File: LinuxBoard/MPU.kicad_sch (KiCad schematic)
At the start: 28 parts, among them J2 Conn_02x10_Counter_Clockwise, J3 Micro_SD_Card, J4 USB_A, SW1 SW_DIP_x03, SW2 SW_Push, SW3 SW_Push, U1 STM32MP151AAB3, Y1 24MHz, Y2 32.768KHz

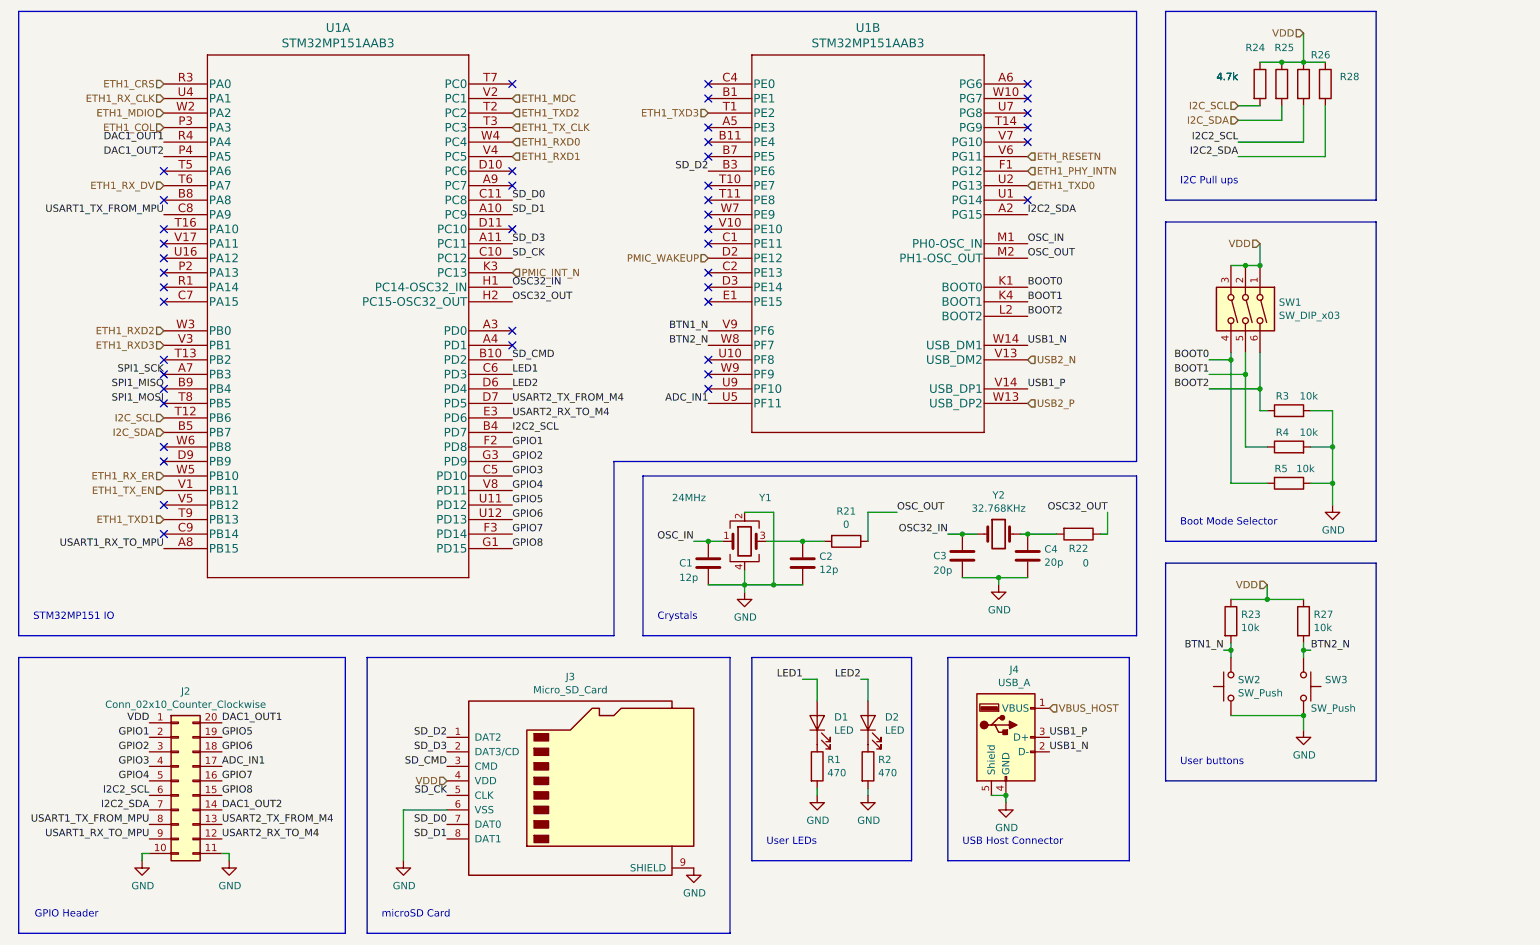
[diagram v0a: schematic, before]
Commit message: Fix ERC errors and reorganize directory
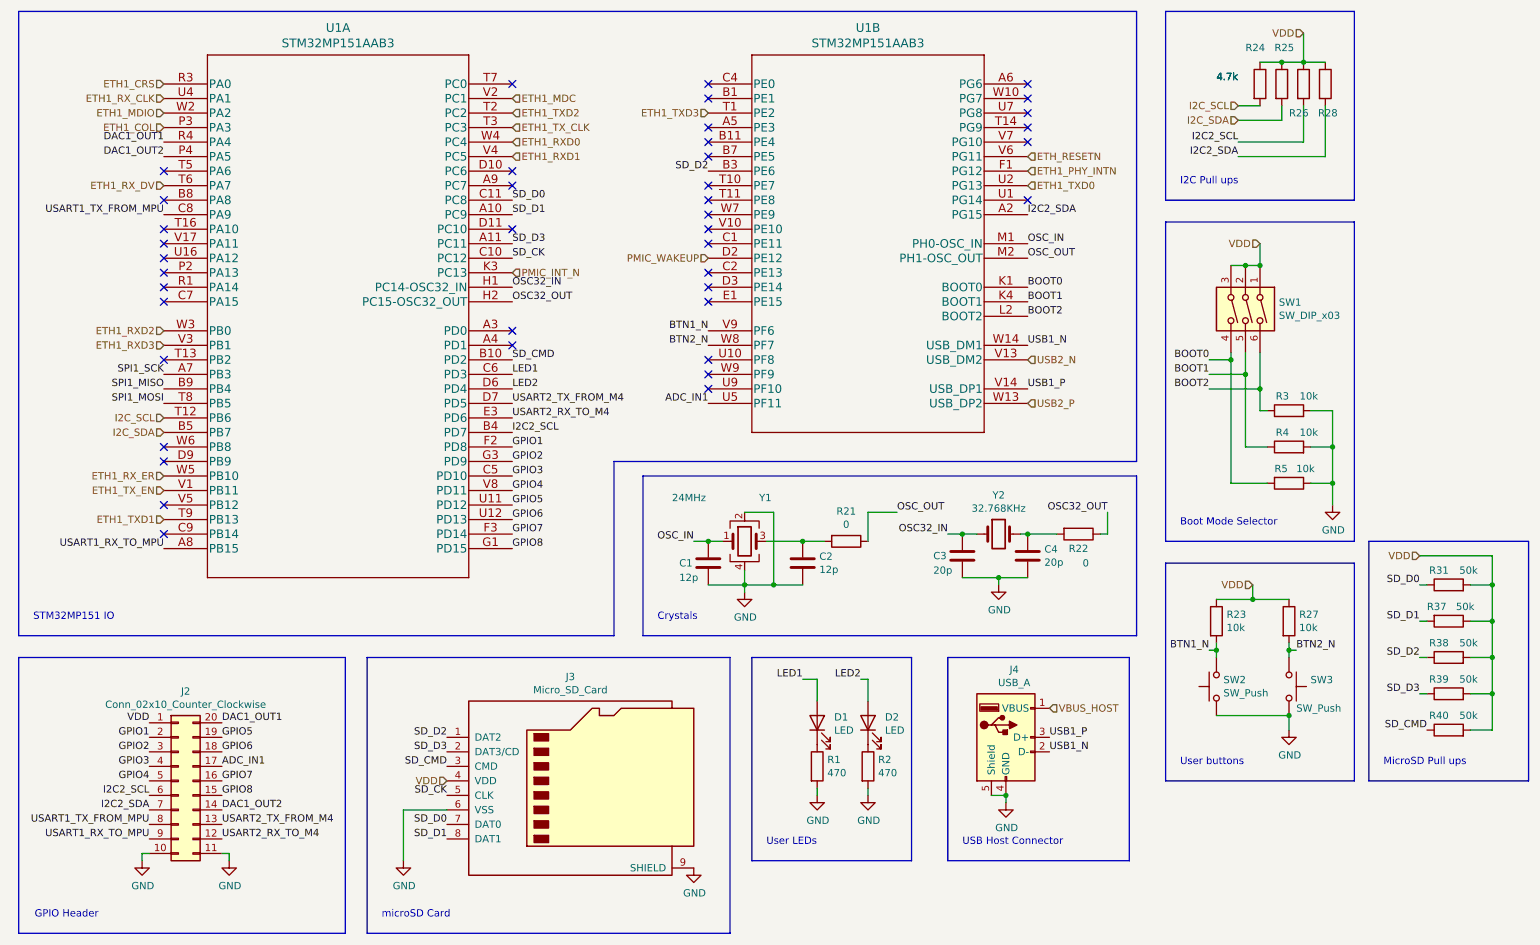
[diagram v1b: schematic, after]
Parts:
- added R31, R37, R38, R39, R40: 50k, Resistor_SMD:R_0603_1608Metric_Pad0.98x0.95mm_HandSolder, symbol Device:R
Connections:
- net SD_CMD: now also R40.1
- net SD_D0: now also R31.1
- net SD_D1: now also R37.2
- net SD_D2: now also R38.1
- net SD_D3: now also R39.1
- net VDD: now also R31.2, R37.1, R38.2, R39.2, R40.2
- no-connect marks 44 -> 41
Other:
- note added: "MicroSD Pull ups"
- moved on the sheet: R23, R27, SW2, SW3

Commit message: Fix resistor footprints, restart layout
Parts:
- R1, R2, R21, R22, R23, R24, R25, R26, R27, R28, R3, R4, R5: footprint Resistor_SMD:R_0603_1608Metric_Pad1.05x0.95mm_HandSolder -> Resistor_SMD:R_0603_1608Metric_Pad0.98x0.95mm_HandSolder
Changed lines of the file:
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@@
       (effects (font (size 1.27 1.27)) (justify left))
     )
-    (property "Footprint" "Resistor_SMD:R_0603_1608Metric_Pad1.05x0.95mm_HandSolder" (id 2) (at 241.3 94.742 90)
+    (property "Footprint" "Resistor_SMD:R_0603_1608Metric_Pad0.98x0.95mm_HandSolder" (id 2) (at 241.3 94.742 90)
       (effects (font (size 1.27 1.27)) hide)
     )
@@
       (effects (font (size 1.27 1.27)) (justify left))
     )
-    (property "Footprint" "Resistor_SMD:R_0603_1608Metric_Pad1.05x0.95mm_HandSolder" (id 2) (at 241.3 91.948 90)
+    (property "Footprint" "Resistor_SMD:R_0603_1608Metric_Pad0.98x0.95mm_HandSolder" (id 2) (at 241.3 91.948 90)
       (effects (font (size 1.27 1.27)) hide)
     )
@@
       (effects (font (size 1.27 1.27)) (justify left))
     )
-    (property "Footprint" "Resistor_SMD:R_0603_1608Metric_Pad1.05x0.95mm_HandSolder" (id 2) (at 241.3 85.598 90)
+    (property "Footprint" "Resistor_SMD:R_0603_1608Metric_Pad0.98x0.95mm_HandSolder" (id 2) (at 241.3 85.598 90)
       (effects (font (size 1.27 1.27)) hide)
     )
@@
       (effects (font (size 1.27 1.27)) (justify left))
     )
-    (property "Footprint" "Resistor_SMD:R_0603_1608Metric_Pad1.05x0.95mm_HandSolder" (id 2) (at 156.972 146.05 90)
+    (property "Footprint" "Resistor_SMD:R_0603_1608Metric_Pad0.98x0.95mm_HandSolder" (id 2) (at 156.972 146.05 90)
       (effects (font (size 1.27 1.27)) hide)
     )
@@
       (effects (font (size 1.27 1.27)) (justify left))
     )
-    (property "Footprint" "Resistor_SMD:R_0603_1608Metric_Pad1.05x0.95mm_HandSolder" (id 2) (at 165.862 146.05 90)
+    (property "Footprint" "Resistor_SMD:R_0603_1608Metric_Pad0.98x0.95mm_HandSolder" (id 2) (at 165.862 146.05 90)
       (effects (font (size 1.27 1.27)) hide)
     )
@@
     (property "Reference" "R22" (id 0) (at 204.47 107.95 90))
     (property "Value" "0" (id 1) (at 205.74 110.49 90))
-    (property "Footprint" "Resistor_SMD:R_0603_1608Metric_Pad1.05x0.95mm_HandSolder" (id 2) (at 204.47 103.632 90)
+    (property "Footprint" "Resistor_SMD:R_0603_1608Metric_Pad0.98x0.95mm_HandSolder" (id 2) (at 204.47 103.632 90)
       (effects (font (size 1.27 1.27)) hide)
     )
@@
     (property "Reference" "R21" (id 0) (at 163.83 101.4222 90))
     (property "Value" "0" (id 1) (at 163.83 103.7336 90))
-    (property "Footprint" "Resistor_SMD:R_0603_1608Metric_Pad1.05x0.95mm_HandSolder" (id 2) (at 163.83 104.902 90)
+    (property "Footprint" "Resistor_SMD:R_0603_1608Metric_Pad0.98x0.95mm_HandSolder" (id 2) (at 163.83 104.902 90)
       (effects (font (size 1.27 1.27)) hide)
     )
@@
       (effects (font (size 1.27 1.27)) (justify left))
     )
-    (property "Footprint" "Resistor_SMD:R_0603_1608Metric_Pad1.05x0.95mm_HandSolder" (id 2) (at 226.822 120.65 90)
+    (property "Footprint" "Resistor_SMD:R_0603_1608Metric_Pad0.98x0.95mm_HandSolder" (id 2) (at 226.822 120.65 90)
       (effects (font (size 1.27 1.27)) hide)
     )
@@
       (effects (font (size 1.27 1.27)) (justify left))
     )
-    (property "Footprint" "Resistor_SMD:R_0603_1608Metric_Pad1.05x0.95mm_HandSolder" (id 2) (at 239.522 120.65 90)
+    (property "Footprint" "Resistor_SMD:R_0603_1608Metric_Pad0.98x0.95mm_HandSolder" (id 2) (at 239.522 120.65 90)
       (effects (font (size 1.27 1.27)) hide)
     )
@@
       (effects (font (size 1.27 1.27)) (justify left))
     )
-    (property "Footprint" "Resistor_SMD:R_0603_1608Metric_Pad1.05x0.95mm_HandSolder" (id 2) (at 234.442 26.67 90)
+    (property "Footprint" "Resistor_SMD:R_0603_1608Metric_Pad0.98x0.95mm_HandSolder" (id 2) (at 234.442 26.67 90)
       (effects (font (size 1.27 1.27)) hide)
     )
@@
       (effects (font (size 1.27 1.27)) (justify left))
     )
-    (property "Footprint" "Resistor_SMD:R_0603_1608Metric_Pad1.05x0.95mm_HandSolder" (id 2) (at 238.252 26.67 90)
+    (property "Footprint" "Resistor_SMD:R_0603_1608Metric_Pad0.98x0.95mm_HandSolder" (id 2) (at 238.252 26.67 90)
       (effects (font (size 1.27 1.27)) hide)
     )
@@
       (effects (font (size 1.27 1.27)) (justify left))
     )
-    (property "Footprint" "Resistor_SMD:R_0603_1608Metric_Pad1.05x0.95mm_HandSolder" (id 2) (at 242.062 26.67 90)
+    (property "Footprint" "Resistor_SMD:R_0603_1608Metric_Pad0.98x0.95mm_HandSolder" (id 2) (at 242.062 26.67 90)
       (effects (font (size 1.27 1.27)) hide)
     )
@@
       (effects (font (size 1.27 1.27)) (justify left))
     )
-    (property "Footprint" "Resistor_SMD:R_0603_1608Metric_Pad1.05x0.95mm_HandSolder" (id 2) (at 245.872 26.67 90)
-      (effects (font (size 1.27 1.27)) hide)
-    )
+    (property "Footprint" "Resistor_SMD:R_0603_1608Metric_Pad0.98x0.95mm_HandSolder" (id 2) (at 245.872 26.67 90)
+      (effects (font (size 1.27 1.27)) hide)
+    )
